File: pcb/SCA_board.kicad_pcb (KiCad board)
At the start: 2 copper layers, 30.1 x 128 mm, 42 parts, among them J1 100616-2, J2 39-29-3086, J3 DIN41612_02x32_AC, J4 USB4145-03-0230-C, J6 USB4145-03-0230-C, J7 Conn_01x03, U1 USBLC6-2SC6, U2 CH340E, U3 M24C02-WMN

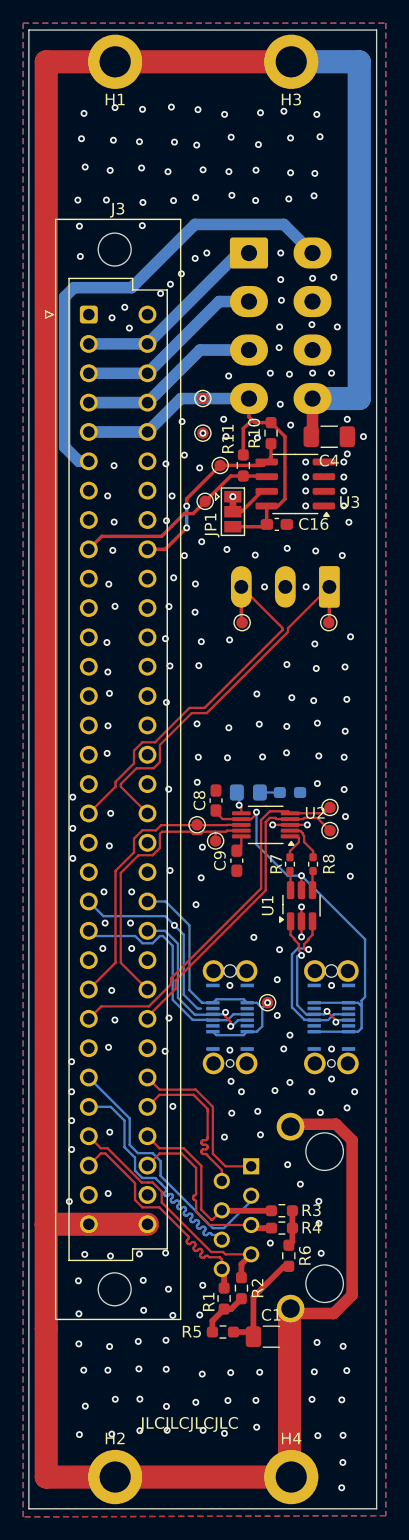
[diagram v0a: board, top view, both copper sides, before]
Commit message: Connector and layout change
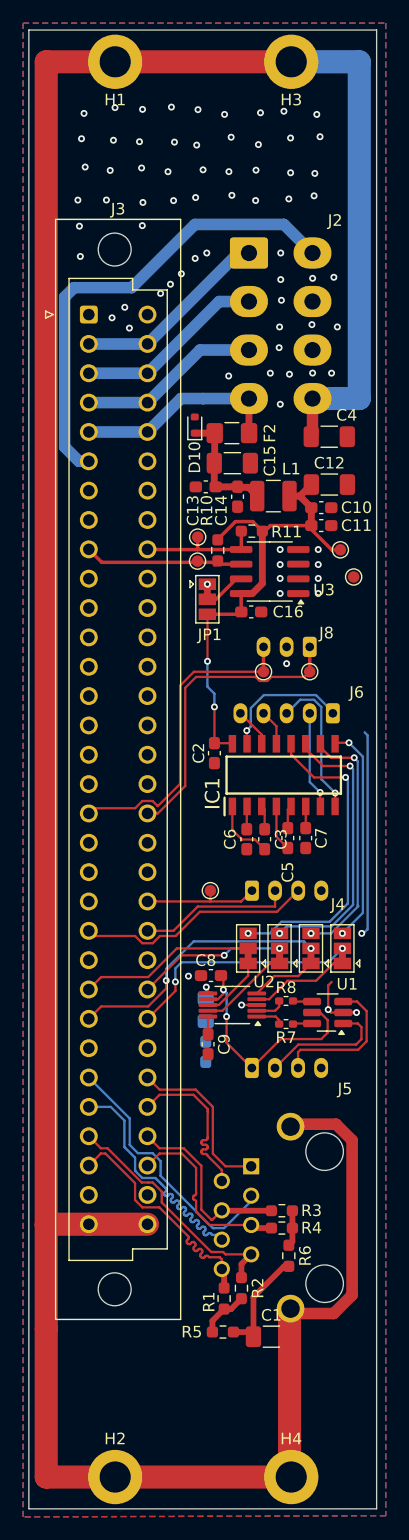
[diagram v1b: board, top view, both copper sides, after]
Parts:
- removed J7: Conn_01x03, Connector_Phoenix_MC:PhoenixContact_MCV_1,5_3-G-3.81_1x03_P3.81mm_Vertical
- removed TP5, TP6, TP7, TP8: TestPoint, TestPoint:TestPoint_Pad_D1.0mm
- added C10: 100n, Capacitor_SMD:C_0603_1608Metric_Pad1.08x0.95mm_HandSolder, F.Cu at (151.2, 74.2)
- added C11: 100n, Capacitor_SMD:C_0603_1608Metric_Pad1.08x0.95mm_HandSolder, F.Cu at (151.2, 75.7)
- added C12: 10u, Capacitor_SMD:C_1206_3216Metric_Pad1.33x1.80mm_HandSolder, F.Cu at (151.9, 72.2)
- added C13: 100n, Capacitor_SMD:C_0603_1608Metric_Pad1.08x0.95mm_HandSolder, F.Cu at (141.2, 72.3)
- added C14: 100n, Capacitor_SMD:C_0603_1608Metric_Pad1.08x0.95mm_HandSolder, F.Cu at (144.0, 73.2)
- added C15: 10u, Capacitor_SMD:C_1206_3216Metric_Pad1.33x1.80mm_HandSolder, F.Cu at (143.6, 70.3)
- added C2: 100n, Capacitor_SMD:C_0603_1608Metric_Pad1.08x0.95mm_HandSolder, F.Cu at (142.0, 95.4)
- added C3: 100n, Capacitor_SMD:C_0603_1608Metric_Pad1.08x0.95mm_HandSolder, F.Cu at (146.3, 102.8)
- added C5: 100n, Capacitor_SMD:C_0603_1608Metric_Pad1.08x0.95mm_HandSolder, F.Cu at (148.3, 102.8)
- added C6: 100n, Capacitor_SMD:C_0603_1608Metric_Pad1.08x0.95mm_HandSolder, F.Cu at (144.8, 102.8)
- added C7: 100n, Capacitor_SMD:C_0603_1608Metric_Pad1.08x0.95mm_HandSolder, F.Cu at (149.9, 102.8)
- added D10: ESD5Z3.3T1G, Diode_SMD:D_SOD-523, F.Cu at (140.3, 67.0)
- added F2: Polyfuse, Fuse:Fuse_1206_3216Metric_Pad1.42x1.75mm_HandSolder, F.Cu at (143.5, 67.7)
- added IC1: ST3232BDR, SamacSys_Parts:SOIC127P600X175-16N, F.Cu at (148.0, 97.3)
- added J5: Conn_01x04_Socket, Connector_JST:JST_PH_B4B-PH-K_1x04_P2.00mm_Vertical, B.Cu at (145.2, 122.7)
- added J8: Conn_01x03_Socket, Connector_JST:JST_PH_B3B-PH-K_1x03_P2.00mm_Vertical, B.Cu at (150.2, 86.2)
- added JP10: SolderJumper_3_Bridged12, Jumper:SolderJumper-3_P1.3mm_Bridged12_Pad1.0x1.5mm, F.Cu at (147.6, 112.3)
- added JP11: SolderJumper_3_Bridged12, Jumper:SolderJumper-3_P1.3mm_Bridged12_Pad1.0x1.5mm, F.Cu at (153.1, 112.3)
- added JP12: SolderJumper_3_Bridged12, Jumper:SolderJumper-3_P1.3mm_Bridged12_Pad1.0x1.5mm, F.Cu at (150.4, 112.3)
- added JP9: SolderJumper_3_Bridged12, Jumper:SolderJumper-3_P1.3mm_Bridged12_Pad1.0x1.5mm, F.Cu at (144.9, 112.3)
- added L1: LQH32PN101MN0L, Inductor_SMD:L_1210_3225Metric, F.Cu at (147.1, 73.2)
- J4: value USB4145-03-0230-C -> Conn_01x04_Socket; footprint SamacSys_Parts:USB4145030230C -> Connector_JST:JST_PH_B4B-PH-K_1x04_P2.00mm_Vertical
- J6: value USB4145-03-0230-C -> Conn_01x05_Socket; footprint SamacSys_Parts:USB4145030230C -> Connector_JST:JST_PH_B5B-PH-K_1x05_P2.00mm_Vertical
- moved J6 26.3 mm to (152.2, 92.0), turned to 180 degrees
- moved D1 23.6 mm to (141.2, 121.2), turned to 90 degrees
- moved R9 19.2 mm to (141.2, 117.6), turned to 90 degrees
- moved TP4 18.0 mm to (154.1, 80.2)
- moved TP11 17.7 mm to (152.9, 77.8)
- moved C9 16.1 mm to (141.4, 120.6)
- moved U2 15.9 mm to (143.6, 117.2)
- moved C8 15.2 mm to (141.7, 114.7), turned to 0 degrees
- moved R7 13.8 mm to (148.2, 118.8), turned to 180 degrees
- moved R8 12.1 mm to (148.2, 116.8), turned to 180 degrees
- moved J4 11.1 mm to (145.2, 107.3), turned to 0 degrees
- moved TP3 10.9 mm to (141.7, 107.3)
- moved U1 9.51 mm to (151.8, 117.8), turned to 180 degrees
- moved R10 8.64 mm to (145.2, 76.2), turned to 0 degrees
- moved C16 7.89 mm to (145.2, 83.2)
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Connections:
- C16 pad 2: /+3,3V_CONN -> +3.3V
- C8 pad 2: Net-(J6-VBUS_1) -> Net-(J5-Pin_1)
- JP1 pad 3: /+3,3V_CONN -> +3.3V
- R10 pad 2: /+3,3V_CONN -> +3.3V
- R11 pad 2: /+3,3V_CONN -> +3.3V
- TP11 pad 1: /+3,3V_CONN -> +3.3V
- U1 pad 5: Net-(J6-VBUS_1) -> Net-(J5-Pin_1)
- U2 pad 4: /RTS -> /USB_RTS
- U2 pad 5: /CTS -> /USB_CTS
- U2 pad 7: Net-(J6-VBUS_1) -> Net-(J5-Pin_1)
- U2 pad 8: /USART- -> /USB_USART-
- U2 pad 9: /USART+ -> /USB_USART+
- U3 pad 8: /+3,3V_CONN -> +3.3V
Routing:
- net +3.3V: track 0.00 -> 42.6 mm, vias 0 -> 2
- net Net-(J6-VBUS_1): track 37.4 -> 0.00 mm, vias 2 -> 0
- net /TTL_USART-: track 0.00 -> 27.3 mm, vias 0 -> 2
- net /TTL_USART+: track 0.00 -> 24.4 mm, vias 0 -> 2
- net /TTL_CTS: track 0.00 -> 21.7 mm, vias 0 -> 2
- net Net-(J5-Pin_1): track 0.00 -> 21.5 mm, vias 0 -> 2
- net /TTL_RTS: track 0.00 -> 19.0 mm, vias 0 -> 2
- net /+3,3V_CONN: track 35.7 -> 18.1 mm, vias 1 -> 0
- net GND: track 22.2 -> 36.1 mm, vias 253 -> 78
- net /VUSB: track 24.2 -> 10.4 mm, vias 1 -> 0
- net /RS232_CTS: track 0.00 -> 12.9 mm, vias 0 -> 1
- net /USART+: track 24.7 -> 12.9 mm, vias 0 -> 2
- net Net-(D10-K): track 0.00 -> 10.4 mm
- net /USART-: track 24.5 -> 15.3 mm
- net /CTS: track 32.4 -> 23.2 mm, vias 0 -> 2
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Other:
- board text added: "+12V"
- board text added: "+3,3V"
- board text added: "+5V"
- board text added: "+5Vsb"
- board text added: "-12V"
- board text added: "ACT"
- board text added: "CTS"
- board text added: "D+"
- board text added: "D-"
- board text added: "GND x3"
- board text added: "RS232"
- board text added: "RTS"
- board text added: "RX"
- board text added: "TX"
- board text added: "USB/UART"
- board text added: "Vbus"
- board text removed: "JLCJLCJLCJLC"
- board text removed: "USB UART"
- board text removed: "USB/UART ACT"

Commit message: Added stitching
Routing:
- net GND: vias 78 -> 240
